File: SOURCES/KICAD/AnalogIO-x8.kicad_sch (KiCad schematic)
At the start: 38 parts

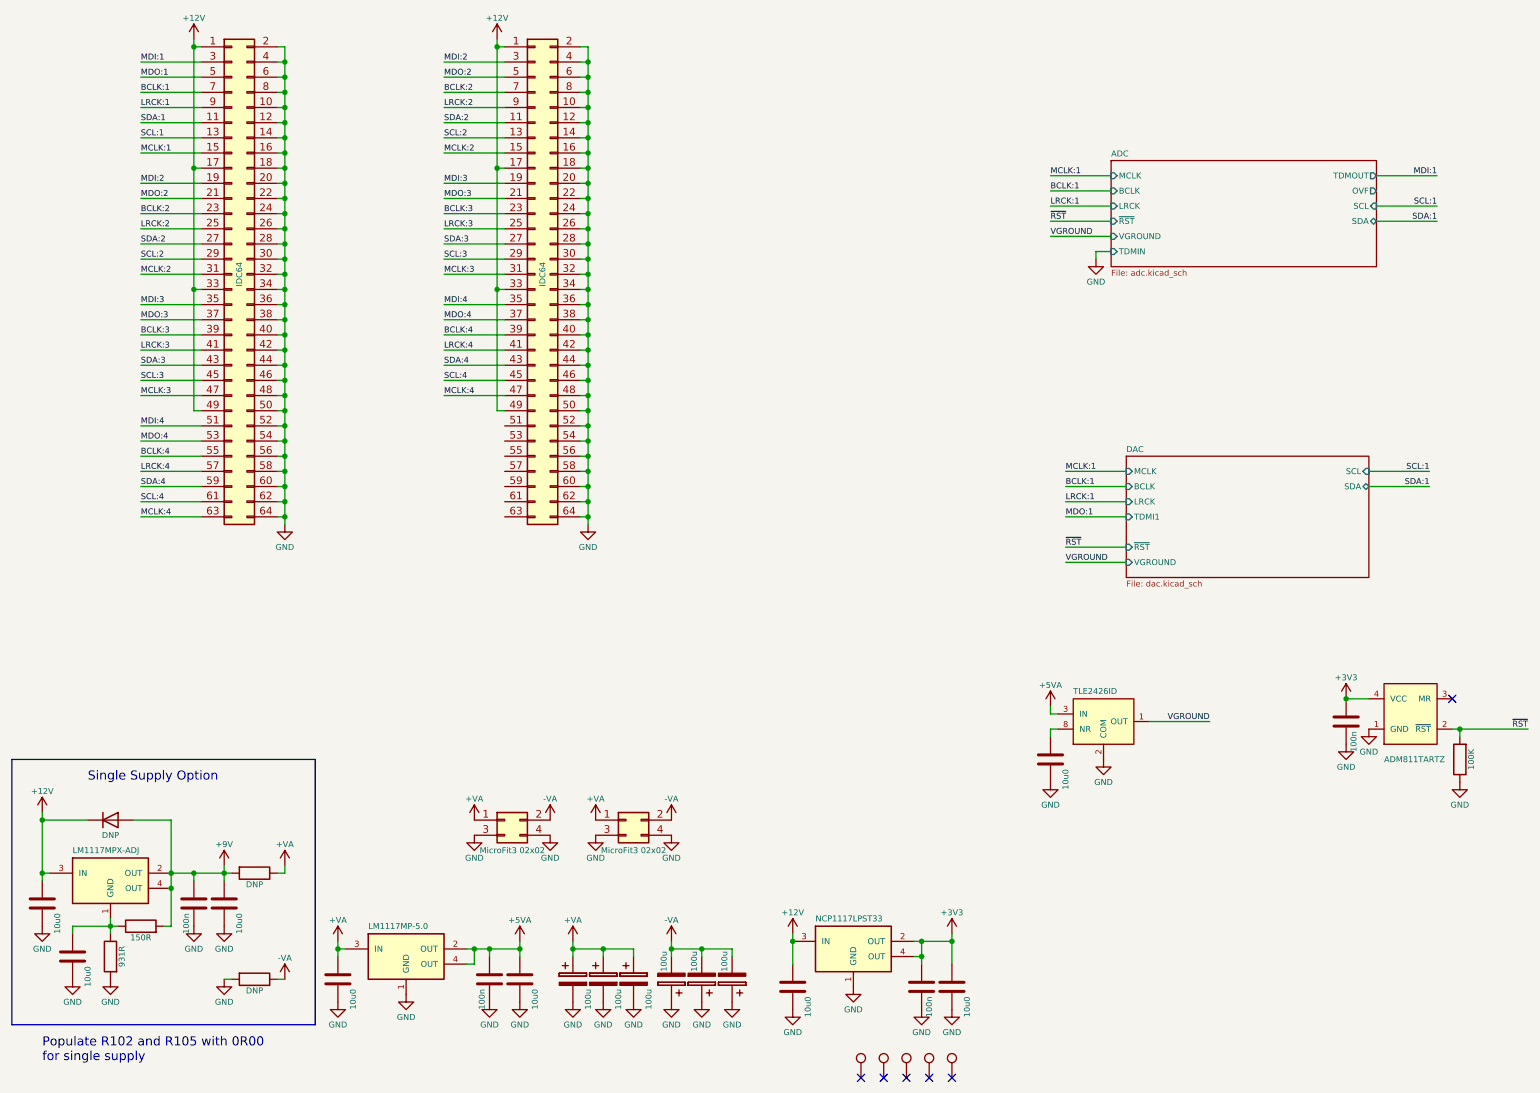
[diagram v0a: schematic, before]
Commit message: Rescue footprints to local library
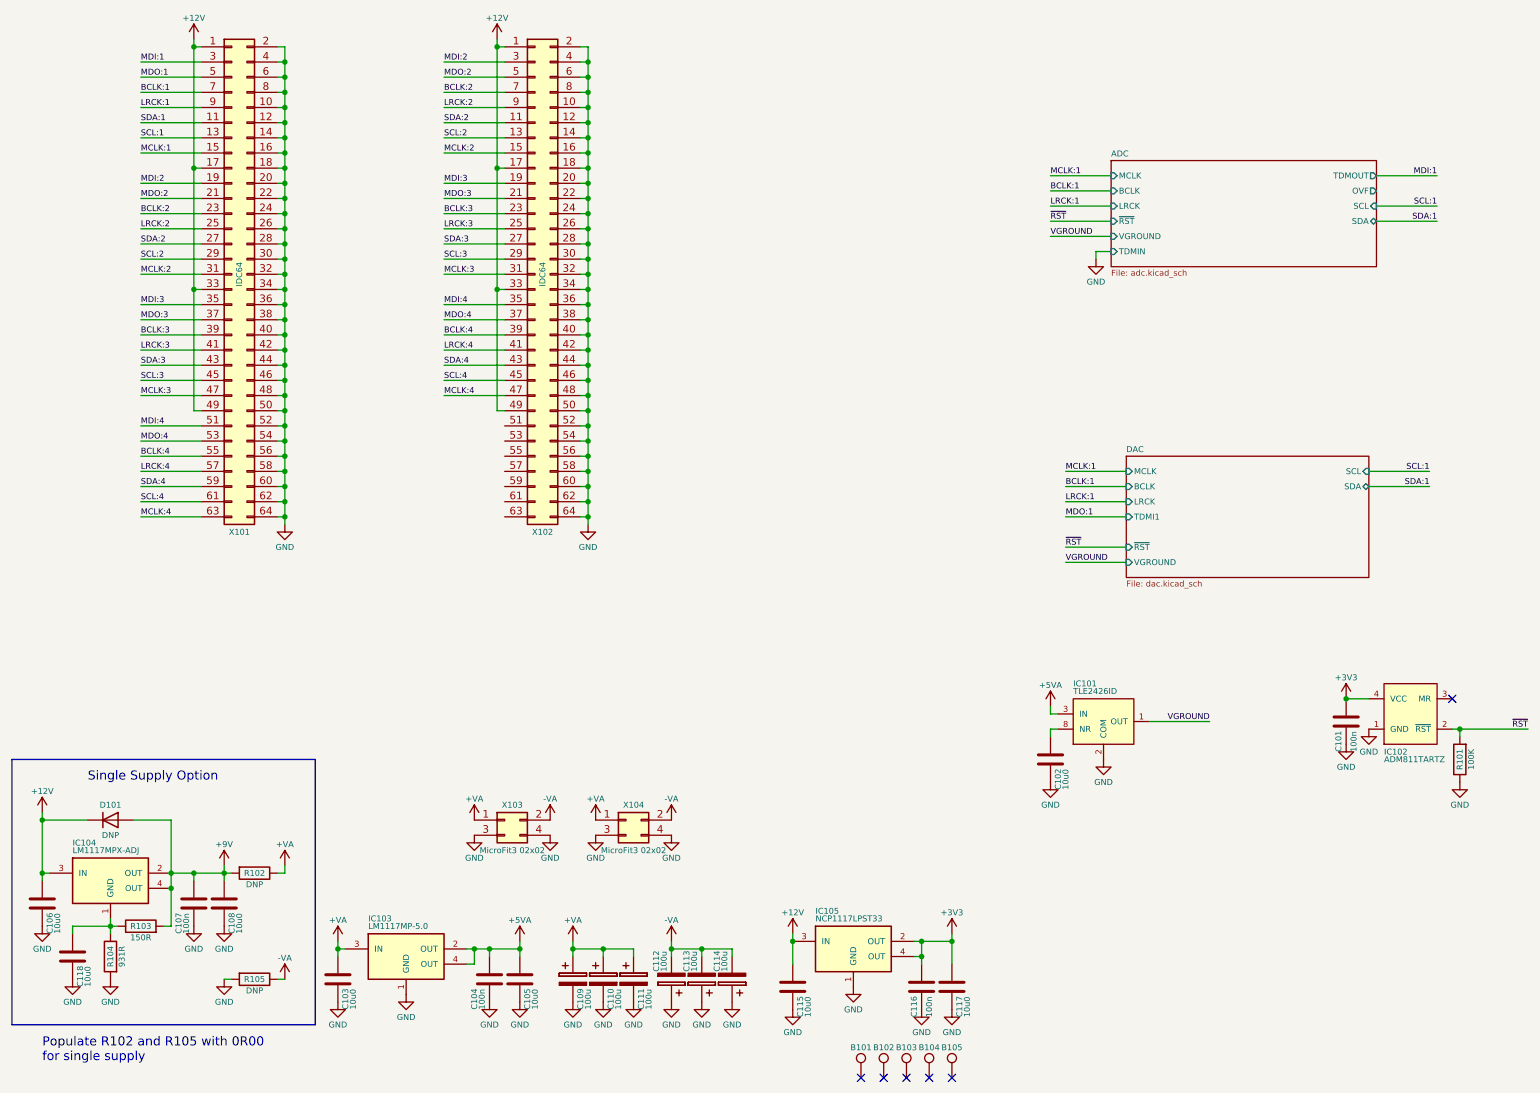
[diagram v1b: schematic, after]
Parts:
- B101, B102, B103, B104, B105: renamed from ?; footprint rklib:MountingHole_3.2mm_M3_DIN965_Pad -> AnalogIO-x8:MountingHole_3.2mm_M3_DIN965_Pad
- C101, C102, C103, C104, C105, C106, C107, C108, C115, C116, C117, C118: renamed from ?; footprint rklib:C0805-X7R -> AnalogIO-x8:C0805-X7R
- C109, C110, C111, C112, C113, C114: renamed from ?; footprint Capacitors_ThroughHole:C_Radial_D5_L11_P2 -> AnalogIO-x8:RD2_D5_L11
- IC101: renamed from ?; footprint Housings_SOIC:SOIC-8_3.9x4.9mm_Pitch1.27mm -> AnalogIO-x8:SOIC8_3.9x4.9mm_Pitch1.27mm
- IC103, IC104, IC105: renamed from ?; footprint TO_SOT_Packages_SMD:SOT-223 -> AnalogIO-x8:SOT223
- X101, X102: renamed from ?; footprint rklib:IDC64 -> AnalogIO-x8:IDC64
- X103, X104: renamed from ?; footprint rklib:Microfit3_43045-0428 -> AnalogIO-x8:Microfit3_43045-0428
- gave numbers to parts that had none: 7
